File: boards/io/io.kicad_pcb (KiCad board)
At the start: 2 copper layers, 100 x 100 mm, 102 parts, among them J1 CU, J2 KB_ROW, J3 KB_COL, U1 74ACT32, U2 74ACT08, U3 74ACT00, U4 AT28C256-PLCC32, U5 62256-TSOP, U6 RC1602A, U7 74AC273, U8 74ACT244

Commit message: Update net lists and PCBs with new part names
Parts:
- D1, D2, D3, D4, D5: value LED -> KP-2012CGCK
- D10, D11, D12, D13, D14, D15, D16, D17, D18, D19, D20, D21, D22, D23, D24, D25, D26, D27, D28, D29, D6, D7, D8, D9: value LED -> KP-2012EC
- J1: value CU -> 61304021021
- R1: value 1 -> 0
- R15, R16, R17, R18, R19, R20, R21, R22, R23, R24, R25, R26, R27, R28, R29, R30, R31, R32, R33, R34, R35, R36, R37, R38: value LED -> 620
- R2, R3, R4, R5, R6: value LED -> 600
- RV1: value 10-20k -> BOURNS 3296Y-1-203LF
- U1: value 74ACT32 -> SN74ACT32PWR
- U2: value 74ACT08 -> SN74ACT08PWR
- U3: value 74ACT00 -> 74ACT00MTCX
- U5: value 62256-TSOP -> CY62256NLL-55ZXI
- U6: value RC1602A -> SSW-116-01-T-S
- U7: value 74AC273 -> MC74AC273DTR2G
- U8: value 74ACT244 -> SN74ACT244PW
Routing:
- net /kb_cp: track 69.5 -> 64.4 mm
- net /~we: track 144.8 -> 144.2 mm

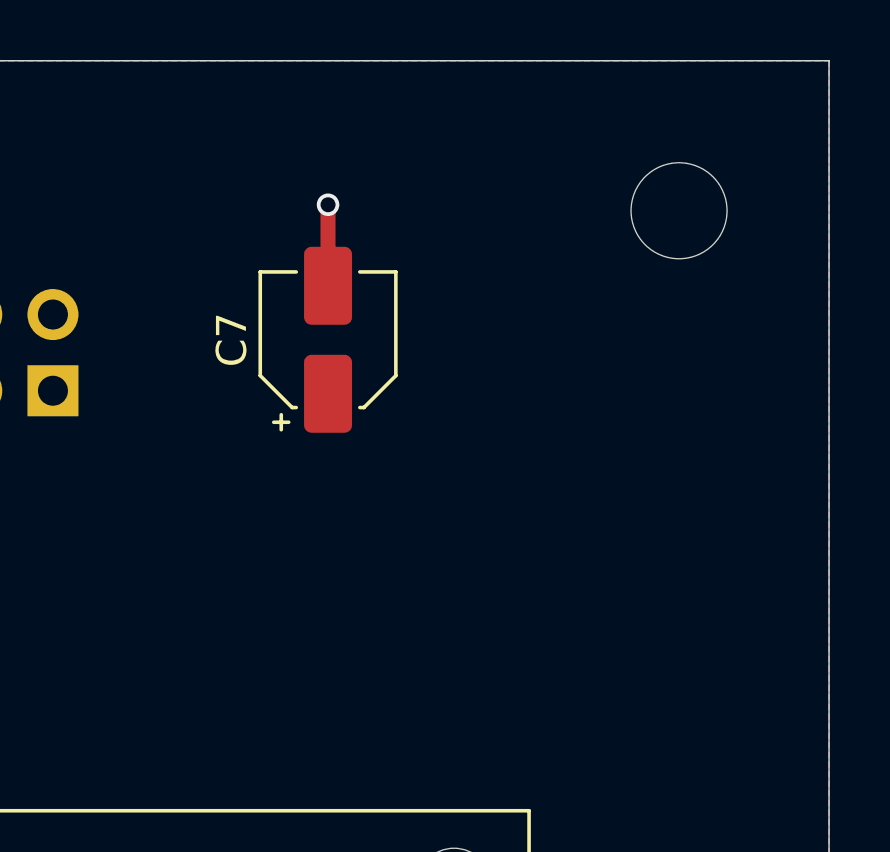
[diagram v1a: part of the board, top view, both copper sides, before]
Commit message: Power connector on the IO board
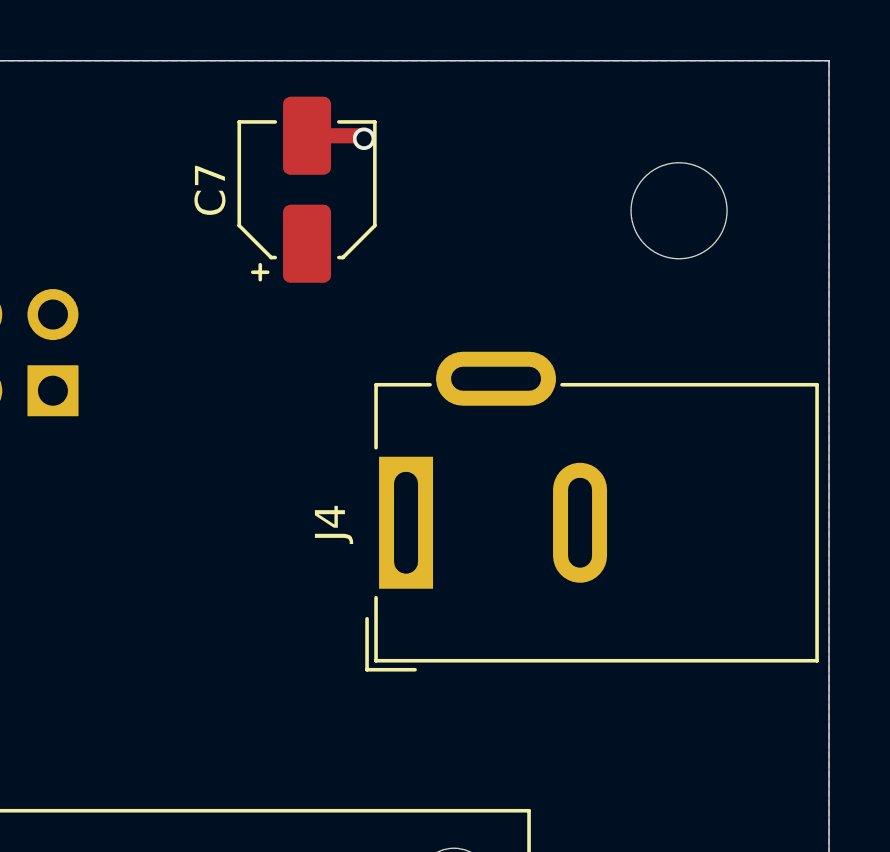
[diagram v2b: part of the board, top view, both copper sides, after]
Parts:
- added J4: Barrel_Jack_Switch, Connector_BarrelJack:BarrelJack_Wuerth_6941xx301002, F.Cu at (185.9, 65.4)
- moved C7 5.05 mm to (182.6, 54.3)
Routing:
- net GND: track 81.4 -> 80.6 mm
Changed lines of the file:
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@@
     (thickness 1.6)
     (drawings 19)
-    (tracks 1219)
+    (tracks 1220)
     (zones 0)
-    (modules 102)
-    (nets 105)
+    (modules 103)
+    (nets 106)
   )
   (page A4)
@@
   )
   (setup
-    (last_trace_width 0.18)
+    (last_trace_width 0.5)
     (user_trace_width 0.5)
     (trace_clearance 0.16)
@@
   (net 103 "Net-(U2-Pad12)")
   (net 104 "Net-(U3-Pad11)")
+  (net 105 "Net-(J4-Pad3)")
   (net_class Default "This is the default net class."
     (clearance 0.16)
@@
     (add_net "Net-(J3-Pad7)")
     (add_net "Net-(J3-Pad8)")
+    (add_net "Net-(J4-Pad3)")
     (add_net "Net-(R1-Pad2)")
     (add_net "Net-(R10-Pad2)")
@@
     (add_net VCC)
   )
+  (module Connector_BarrelJack:BarrelJack_Wuerth_6941xx301002 (layer F.Cu)
+    (at 185.9 65.4 90)
+    (descr "Wuerth electronics barrel jack connector (5.5mm outher diameter, inner diameter 2.05mm or 2.55mm depending on exact order number), See: http://katalog.we-online.de/em/datasheet/6941xx301002.pdf")
+    (tags "connector barrel jack")
+    (fp_text reference J4 (at 0 -2.5 90) (layer F.SilkS)
+      (effects (font (size 1 1) (thickness 0.15)))
+    )
+    (fp_text value Barrel_Jack_Switch (at 0 15.5 90) (layer F.Fab)
+      (effects (font (size 1 1) (thickness 0.15)))
+    )
+    (fp_line (start -4.6 -1) (end -2.5 -1) (layer F.SilkS) (width 0.12))
+    (fp_line (start 6.2 0.5) (end 5 0.5) (layer F.CrtYd) (width 0.05))
+    (fp_line (start 6.2 5.5) (end 5 5.5) (layer F.CrtYd) (width 0.05))
+    (fp_line (start 6.2 0.5) (end 6.2 5.5) (layer F.CrtYd) (width 0.05))
+    (fp_line (start 5 0.5) (end 5 -1.4) (layer F.CrtYd) (width 0.05))
+    (fp_line (start -5 14.1) (end 5 14.1) (layer F.CrtYd) (width 0.05))
+    (fp_line (start -5 -1.4) (end -5 14.1) (layer F.CrtYd) (width 0.05))
+    (fp_line (start 5 -1.4) (end -5 -1.4) (layer F.CrtYd) (width 0.05))
+    (fp_line (start -4.9 -1.3) (end -4.9 0.3) (layer F.SilkS) (width 0.12))
+    (fp_line (start -3.2 -1.3) (end -4.9 -1.3) (layer F.SilkS) (width 0.12))
+    (fp_line (start 4.6 -1) (end 4.6 0.8) (layer F.SilkS) (width 0.12))
+    (fp_line (start 2.5 -1) (end 4.6 -1) (layer F.SilkS) (width 0.12))
+    (fp_line (start -4.6 13.7) (end -4.6 -1) (layer F.SilkS) (width 0.12))
+    (fp_line (start 4.6 13.7) (end -4.6 13.7) (layer F.SilkS) (width 0.12))
+    (fp_text user %R (at 0 7.5 90) (layer F.Fab)
+      (effects (font (size 1 1) (thickness 0.15)))
+    )
+    (fp_line (start -4.5 13.6) (end -4.5 0.1) (layer F.Fab) (width 0.1))
+    (fp_line (start 4.5 13.6) (end -4.5 13.6) (layer F.Fab) (width 0.1))
+    (fp_line (start 4.5 -0.9) (end 4.5 13.6) (layer F.Fab) (width 0.1))
+    (fp_line (start 4.5 -0.9) (end -3.5 -0.9) (layer F.Fab) (width 0.1))
+    (fp_line (start -4.5 0.1) (end -3.5 -0.9) (layer F.Fab) (width 0.1))
+    (fp_line (start 4.6 5.2) (end 4.6 13.7) (layer F.SilkS) (width 0.12))
+    (fp_line (start 5 14.1) (end 5 5.5) (layer F.CrtYd) (width 0.05))
+    (pad 1 thru_hole rect (at 0 0 90) (size 4.4 1.8) (drill oval 3.4 0.8) (layers *.Cu *.Mask)
+      (net 1 VCC))
+    (pad 2 thru_hole oval (at 0 5.8 90) (size 4 1.8) (drill oval 3 0.8) (layers *.Cu *.Mask)
+      (net 2 GND))
+    (pad 3 thru_hole oval (at 4.8 3 180) (size 4 1.8) (drill oval 3 0.8) (layers *.Cu *.Mask)
+      (net 105 "Net-(J4-Pad3)"))
+    (model ${KISYS3DMOD}/Connector_BarrelJack.3dshapes/BarrelJack_Wuerth_6941xx301002.wrl
+      (at (xyz 0 0 0))
+      (scale (xyz 1 1 1))
+      (rotate (xyz 0 0 0))
+    )
+  )
   (module MountingHole:MountingHole_2.5mm (layer F.Cu)
     (at 112.5 108.5)
@@
   )
   (module Capacitor_SMD:CP_Elec_4x4.5 (layer F.Cu)
-    (at 183.3 59.3 90)
+    (at 182.6 54.3 90)
     (descr "SMD capacitor, aluminum electrolytic, Nichicon, 4.0x4.5mm")
     (tags "capacitor electrolytic")
@@
   (segment (start 162.35 137.55) (end 163.4 138.6) (width 0.18) (layer F.Cu) (net 1))
   (segment (start 162.35 135.425) (end 162.35 137.55) (width 0.18) (layer F.Cu) (net 1))
-  (via (at 183.3 54.8) (size 0.75) (drill 0.5) (layers F.Cu B.Cu) (net 2))
-  (segment (start 183.3 57.5) (end 183.3 54.8) (width 0.5) (layer F.Cu) (net 2) (status 10))
   (via (at 157.5 86.8) (size 0.75) (drill 0.5) (layers F.Cu B.Cu) (net 2))
   (segment (start 157.55 86.75) (end 157.5 86.8) (width 0.5) (layer F.Cu) (net 2))
@@
   (via (at 163 74.2) (size 0.5) (drill 0.3) (layers F.Cu B.Cu) (net 2))
   (segment (start 163 72.9375) (end 163 74.2) (width 0.18) (layer F.Cu) (net 2))
+  (via (at 184.5 52.6) (size 0.75) (drill 0.5) (layers F.Cu B.Cu) (net 2))
+  (segment (start 184.4 52.5) (end 184.5 52.6) (width 0.5) (layer F.Cu) (net 2))
+  (segment (start 182.6 52.5) (end 184.4 52.5) (width 0.5) (layer F.Cu) (net 2))
   (segment (start 107.9375 120) (end 110.0625 120) (width 0.18) (layer F.Cu) (net 3) (status 30))
   (via (at 165.3 79.8) (size 0.5) (drill 0.3) (layers F.Cu B.Cu) (net 4))

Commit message: Add license information
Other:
- board text added: "Licensed under the TAPR OHL (www.tapr.org/OHL)"
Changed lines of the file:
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@@
   (general
     (thickness 1.6)
-    (drawings 19)
+    (drawings 20)
     (tracks 1220)
     (zones 0)
@@
     (date 2020-02-29)
     (rev 1)
+    (comment 1 "Licensed under the TAPR Open Hardware License (www.tapr.org/OHL)")
   )
   (layers
@@
     )
   )
+  (gr_text "Licensed under the TAPR OHL\n(www.tapr.org/OHL)" (at 184.1 91.8) (layer B.SilkS)
+    (effects (font (size 1 1) (thickness 0.15)) (justify mirror))
+  )
   (gr_text IO (at 114.5 132) (layer F.SilkS)

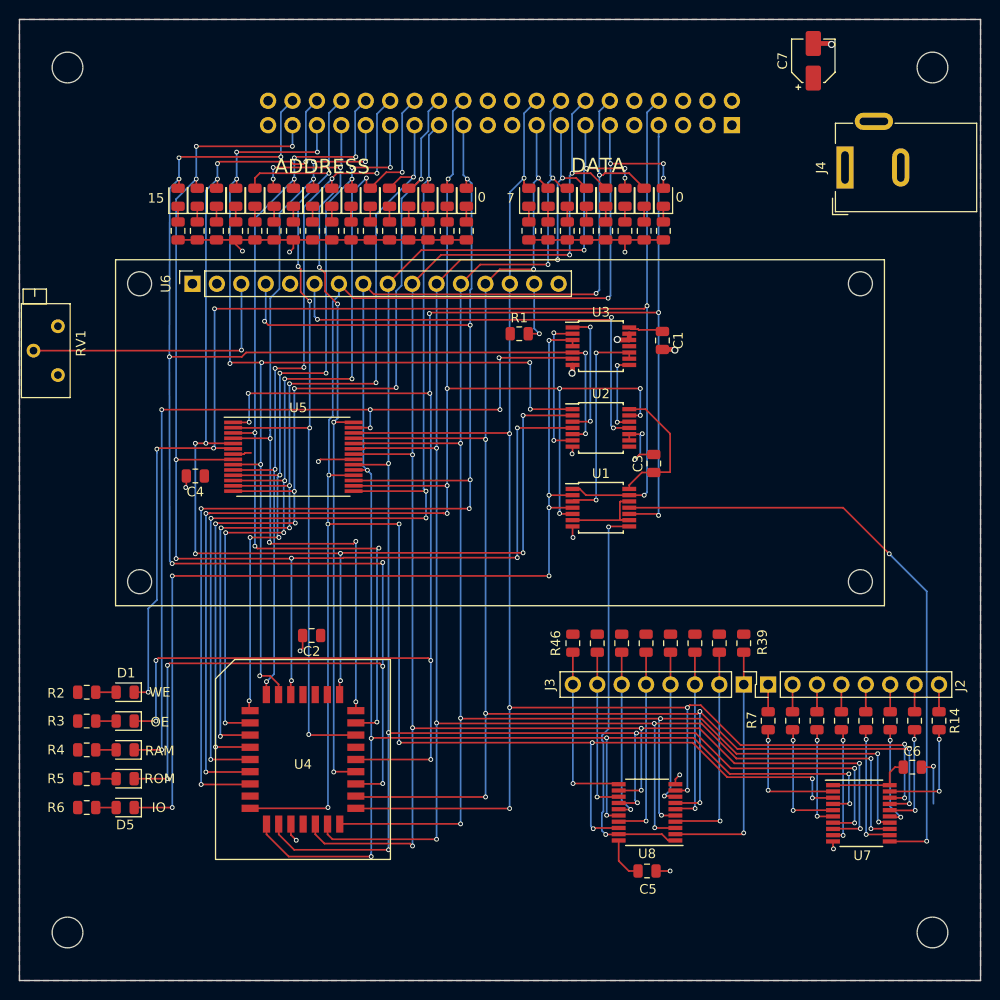
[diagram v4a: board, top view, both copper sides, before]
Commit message: Fix swapped ROM pins
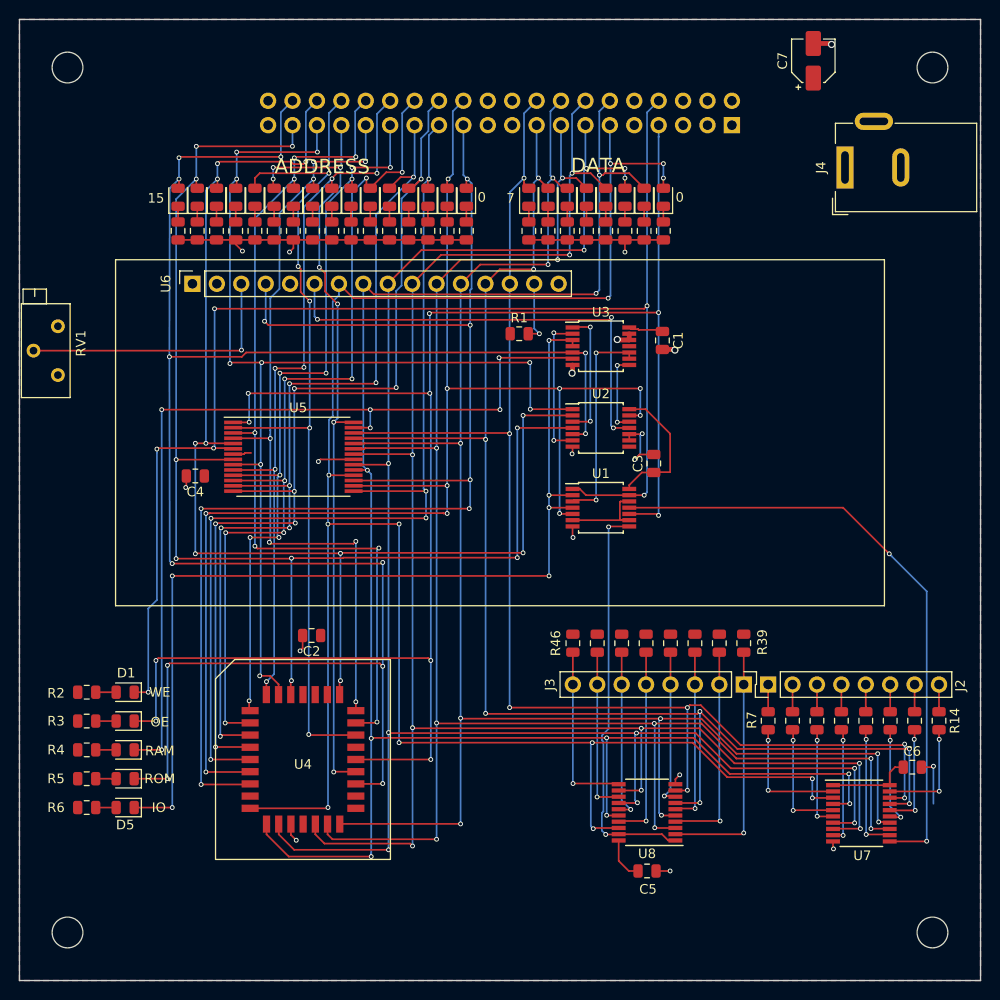
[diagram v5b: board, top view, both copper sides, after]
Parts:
- removed REF** (x4): MountingHole_2.5mm, MountingHole:MountingHole_2.5mm
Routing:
- net /d7: track 168.3 -> 141.8 mm, vias 8 -> 7
- net /d6: track 168.8 -> 146.6 mm, vias 9 -> 8

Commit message: IO: PCB rev. 2
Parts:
- removed C1: 0.1u, Capacitor_SMD:C_0805_2012Metric
- removed J3: KB_COL, Connector_PinHeader_2.54mm:PinHeader_1x08_P2.54mm_Vertical
- removed RV1: BOURNS 3296Y-1-203LF, Potentiometer_THT:Potentiometer_Bourns_3296Z_Horizontal
- removed U3: 74ACT00MTCX, Package_SO:TSSOP-14_4.4x5mm_P0.65mm
- removed U6: SSW-116-01-T-S, Connector_PinSocket_2.54mm:PinSocket_1x16_P2.54mm_Vertical
- added C12: 0.1u, Capacitor_SMD:C_0805_2012Metric, F.Cu at (126.5, 84.1)
- added C13: 0.1u, Capacitor_SMD:C_0805_2012Metric, F.Cu at (134.8, 126.8)
- added C14: 0.1u, Capacitor_SMD:C_0805_2012Metric, F.Cu at (124.2, 128.3)
- added C16: 0.1u, Capacitor_SMD:C_0805_2012Metric, F.Cu at (148.6, 116.4)
- added C8: 0.1u, Capacitor_SMD:C_0805_2012Metric, F.Cu at (148.8, 126.6)
- added C9: 0.1u, Capacitor_SMD:C_0805_2012Metric, F.Cu at (142.0, 84.4)
- added D30: KP-2012EC, LED_SMD:LED_0805_2012Metric, F.Cu at (143.9, 134.7)
- added D31: KP-2012EC, LED_SMD:LED_0805_2012Metric, F.Cu at (143.9, 137.8)
- added D32: KP-2012EC, LED_SMD:LED_0805_2012Metric, F.Cu at (143.9, 140.8)
- added D33: KP-2012EC, LED_SMD:LED_0805_2012Metric, F.Cu at (143.9, 143.8)
- added D34: KP-2012EC, LED_SMD:LED_0805_2012Metric, F.Cu at (143.9, 146.8)
- added D35: KP-2012EC, LED_SMD:LED_0805_2012Metric, F.Cu at (196.8, 81.0)
- added D36: KP-2012EC, LED_SMD:LED_0805_2012Metric, F.Cu at (104.4, 81.0)
- added D37: KP-2012EC, LED_SMD:LED_0805_2012Metric, F.Cu at (148.0, 96.4)
- added J5: Conn_01x08, Connector_PinHeader_2.54mm:PinHeader_1x08_P2.54mm_Vertical, F.Cu at (177.8, 138.5)
- added J6: SSW-120-02-G-D-RA, Connector_PinSocket_2.54mm:PinSocket_2x20_P2.54mm_Horizontal, B.Cu at (189.0, 75.9)
- added J7: Conn_01x08, Connector_PinHeader_2.54mm:PinHeader_1x08_P2.54mm_Vertical, F.Cu at (175.3, 138.5)
- added R47: 620, Resistor_SMD:R_0805_2012Metric, F.Cu at (147.7, 137.8)
- added R48: 620, Resistor_SMD:R_0805_2012Metric, F.Cu at (147.7, 140.7)
- added R49: 620, Resistor_SMD:R_0805_2012Metric, F.Cu at (147.7, 143.8)
- added R50: 620, Resistor_SMD:R_0805_2012Metric, F.Cu at (147.7, 146.8)
- added R51: 620, Resistor_SMD:R_0805_2012Metric, F.Cu at (196.8, 78.8)
- added R52: 620, Resistor_SMD:R_0805_2012Metric, F.Cu at (104.4, 78.8)
- added R53: 620, Resistor_SMD:R_0805_2012Metric, F.Cu at (148.0, 92.6)
- added U10: MC74HC151ADTR2G, Package_SO:TSSOP-16_4.4x5mm_P0.65mm, F.Cu at (130.6, 124.5)
- added U11: SN74LV273APW, Package_SO:TSSOP-20_4.4x6.5mm_P0.65mm, F.Cu at (143.8, 124.4)
- added U13: IS61C256AL-12TLI, Package_SO:TSOP-I-28_11.8x8mm_P0.55mm, F.Cu at (141.8, 94.5)
- added U14: SN74LV139APW, Package_SO:TSSOP-16_4.4x5mm_P0.65mm, F.Cu at (144.1, 114.0)
- added U9: 74HC30D, Package_SO:SOIC-14_3.9x8.7mm_P1.27mm, F.Cu at (119.9, 82.0)
- C7: footprint Capacitor_SMD:CP_Elec_4x4.5 -> Capacitor_Tantalum_SMD:CP_EIA-3528-21_Kemet-B_Pad1.50x2.35mm_HandSolder
- J2: value KB_ROW -> SSW-120-02-G-D-RA; footprint Connector_PinHeader_2.54mm:PinHeader_1x08_P2.54mm_Vertical -> Connector_PinSocket_2.54mm:PinSocket_2x20_P2.54mm_Horizontal; moved to B.Cu
- J4: value Barrel_Jack_Switch -> 694106301002
- R1: value 0 -> 620
- U1: value SN74ACT32PWR -> 74LV32APWJ
- U2: value SN74ACT08PWR -> SN74LV00APW
- U5: value CY62256NLL-55ZXI -> IS61C256AL-12TLI
- U7: value MC74AC273DTR2G -> SN74LV273APW
- U8: value SN74ACT244PW -> SN74LV244APW
- moved C7 112.5 mm to (104.0, 134.8)
- moved J4 98.0 mm to (118.0, 136.0), turned to 0 degrees
- moved J2 67.1 mm to (111.0, 124.1), turned to 0 degrees
- moved U2 52.5 mm to (120.0, 125.9), turned to 270 degrees
- moved R1 52.2 mm to (147.7, 134.7), turned to 180 degrees
- moved C2 51.7 mm to (170.0, 80.8), turned to 0 degrees
- moved U4 51.2 mm to (167.8, 93.0)
- moved C4 38.4 mm to (108.0, 134.5), turned to 90 degrees
- moved R46 28.0 mm to (157.4, 142.9), turned to 270 degrees
- moved R45 28.0 mm to (159.9, 142.9), turned to 270 degrees
- moved R44 28.0 mm to (162.5, 142.9), turned to 270 degrees
- moved R43 28.0 mm to (165.0, 142.9), turned to 270 degrees
- moved R42 28.0 mm to (167.6, 142.9), turned to 270 degrees
- moved R41 28.0 mm to (170.1, 142.9), turned to 270 degrees
- moved R40 28.0 mm to (172.7, 142.9), turned to 270 degrees
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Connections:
- net /~ram_cs renamed /~ramh_cs
- J1 pad 5: GND -> /~rdy
- J2 pad 1: Net-(J2-Pad1) -> VCC
- J2 pad 2: Net-(J2-Pad2) -> GND
- J2 pad 4: Net-(J2-Pad4) -> /~rst
- J2 pad 5: Net-(J2-Pad5) -> /~rdy
- J2 pad 6: Net-(J2-Pad6) -> /l_ena
- J2 pad 7: Net-(J2-Pad7) -> /~oe
- J2 pad 8: Net-(J2-Pad8) -> /~we
- R1 pad 1: VCC -> GND
- R10 pad 1: Net-(J2-Pad4) -> Net-(J5-Pad4)
- R11 pad 1: Net-(J2-Pad5) -> Net-(J5-Pad5)
- R12 pad 1: Net-(J2-Pad6) -> Net-(J5-Pad6)
- R13 pad 1: Net-(J2-Pad7) -> Net-(J5-Pad7)
- R14 pad 1: Net-(J2-Pad8) -> Net-(J5-Pad8)
- R7 pad 1: Net-(J2-Pad1) -> Net-(J5-Pad1)
- R8 pad 1: Net-(J2-Pad2) -> Net-(J5-Pad2)
- R9 pad 1: Net-(J2-Pad3) -> Net-(J5-Pad3)
- U1 pad 2: /~io_cs -> /~cr_cs
- U1 pad 3: Net-(U1-Pad3) -> /cr_cp
- U1 pad 4: /~io_cs -> /a15
- U1 pad 5: /a1 -> /raml_ena
- U1 pad 6: /~kb_cs -> /~rom_cs
- U2 pad 1: /a12 -> /a15
- U2 pad 10: GND -> VCC
- U2 pad 11: /lcd_e -> Net-(U2-Pad11)
- U2 pad 12: Net-(U2-Pad12) -> VCC
- U2 pad 13: /a1 -> VCC
- U2 pad 2: /a13 -> /a15
- U2 pad 3: Net-(U2-Pad3) -> /~a15
- U2 pad 4: /a14 -> /~a15
- U2 pad 5: /a15 -> /raml_ena
- U2 pad 6: Net-(U2-Pad6) -> /~raml_cs
- U2 pad 9: GND -> VCC
- U4 pad 23: /a15 -> /~rom_cs
- U7 pad 1: VCC -> /~rst
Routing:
- net GND: track 80.6 -> 904.6 mm, vias 19 -> 57
- net VCC: track 33.5 -> 659.4 mm, vias 0 -> 13
- net /~rst: track 0.00 -> 160.4 mm, vias 0 -> 6
- net /~rdy: track 0.00 -> 139.8 mm, vias 0 -> 7
- net /r_ena: track 0.00 -> 89.6 mm, vias 0 -> 3
- net /a12: track 114.0 -> 202.4 mm, vias 9 -> 12
- net /a10: track 82.8 -> 167.1 mm, vias 7 -> 10
- net /a7: track 76.7 -> 158.3 mm, vias 6 -> 8
- net /~we: track 144.2 -> 225.8 mm, vias 6 -> 9
- net /l_ena: track 0.00 -> 80.3 mm, vias 0 -> 2
- net /raml_ena: track 0.00 -> 79.0 mm, vias 0 -> 7
- net /a8: track 82.4 -> 158.7 mm, vias 7 -> 10
- net /a6: track 80.0 -> 155.6 mm, vias 9 -> 8
- net /a13: track 130.7 -> 203.3 mm, vias 10 -> 12
- net /a9: track 91.6 -> 162.2 mm, vias 7 -> 9
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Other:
- board text added: "A000"
- board text added: "B000"
- board text added: "C000"
- board text added: "D000"
- board text added: "E000"
- board text added: "Hi"
- board text added: "Hi RAM 8000-EFFF"
- board text added: "IO rev.2"
- board text added: "Lo"
- board text added: "Lo RAM 0000-7FFF"
- board text added: "RAM seg"
- board text removed: "RAM"
- board text removed: "ROM"
